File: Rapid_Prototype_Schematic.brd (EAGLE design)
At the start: 142 x 95 mm, 169 parts, among them IC2 SI4459ADY-T1-GE3, IC8 SI4485DY-T1-GE3, J1 XT60-M, J10 XT60-M, J2 XT60-M, J3 Vertical Qwiic Connector, J4 UJ2-MIBH-2-SMT-TR-67, J5 XT60-M, J6 XT60-M, J7 XT60-M, J8 XT60-M, J9 XT60-M, Q1 LTV-8141S, Q10 SI4435DDY, Q11 DMN65D8LFB-7, Q12 SI4435DDY, Q13 DMN65D8LFB-7, Q14 SI4435DDY, Q15 DMN65D8LFB-7, Q16 2N7002PW, Q2 2N7002PW, Q3 DMN65D8LFB-7, Q4 SI4435DDY, Q5 DMN65D8LFB-7, Q6 SI4435DDY, Q7 DMN65D8LFB-7, Q8 SI4435DDY, Q9 DMN65D8LFB-7, U1 LM35DM, U2 LM2904ITPX/NOPB, U3 LM2904ITPX/NOPB, U4 LM2904ITPX/NOPB, U5 LM2904ITPX/NOPB, U6 LM2904ITPX/NOPB, U7 TLV1117LV33DCYR, U8 LT1374IS8-5PBF

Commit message: Added Regulator Library, and Regulator to the Level shifter
Changed 5 volt traces from 0.008 to 0.02 for more flow.
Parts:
- removed L3: 10μH, SparkFun-Coils:0805
- added L1: SRR1206-5R0ML, INDUCTOR_SRR1240:IND_BOURNS_SRR1240
- moved C34 5.08 mm to (54.5, 22.5)
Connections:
- net 5V: now also L1.1; no longer L3.2
- net N$3: now also L1.2; no longer L3.1
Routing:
- net 5V: track 387.7 -> 370.4 mm, vias 13 -> 14
- net TETHER_A: track 83.7 -> 86.9 mm

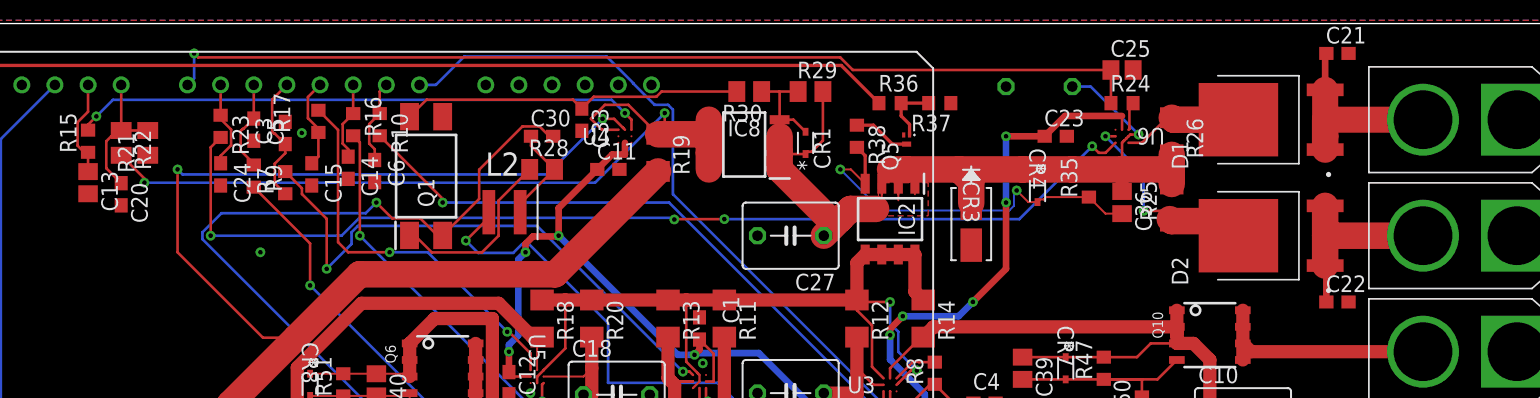
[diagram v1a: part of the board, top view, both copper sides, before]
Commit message: POLYGONS!!!
worked on creating polygons for the high current traces
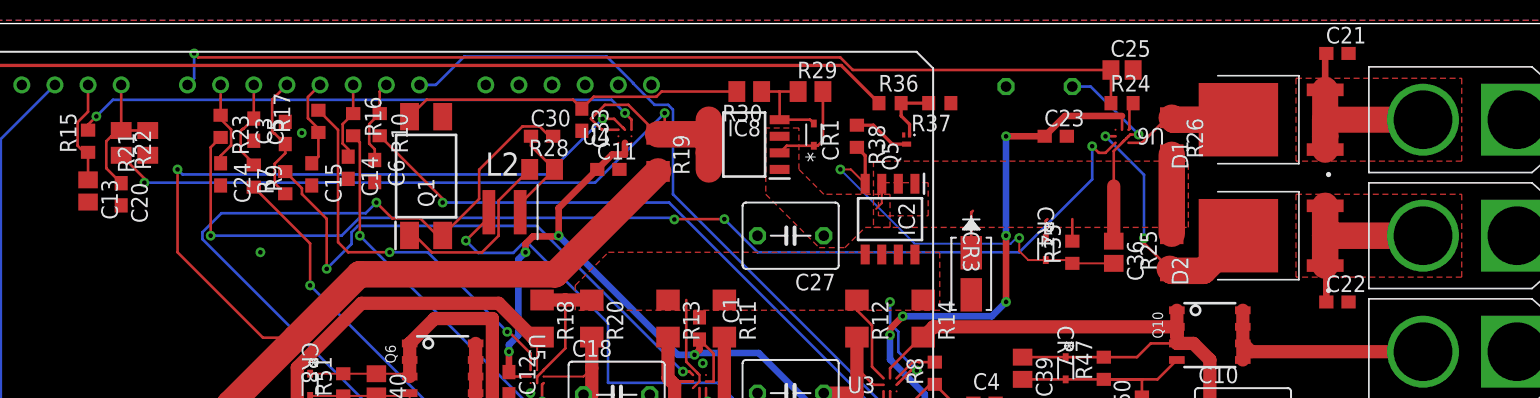
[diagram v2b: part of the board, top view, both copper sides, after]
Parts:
- moved R35 5.24 mm to (101.6, 77.5)
- moved CR4 4.49 mm to (99.6, 77.7)
- moved C36 3.86 mm to (104.8, 77.5)
- moved CR3 3.81 mm to (93.9, 75.8)
- moved R25 3.81 mm to (109.2, 77.5)
- moved CR1 0.90 mm to (81.8, 86.5)
- moved C13 0.64 mm to (26.2, 82.2)
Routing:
- net ESC_POWER: track 67.6 -> 33.6 mm
- net COMBINED_POWER: track 72.2 -> 39.3 mm
- net ESC_POWER2: track 16.0 -> 19.6 mm
- net N$34: track 80.7 -> 84.3 mm
- net 5V: track 370.4 -> 371.9 mm
- net ELEC_CURR: track 7.50 -> 8.17 mm
- added copper zone on layer 1, net ESC_POWER
- added copper zone on layer 1, net P_BATT+
- added copper zone on layer 1, net S_BATT+

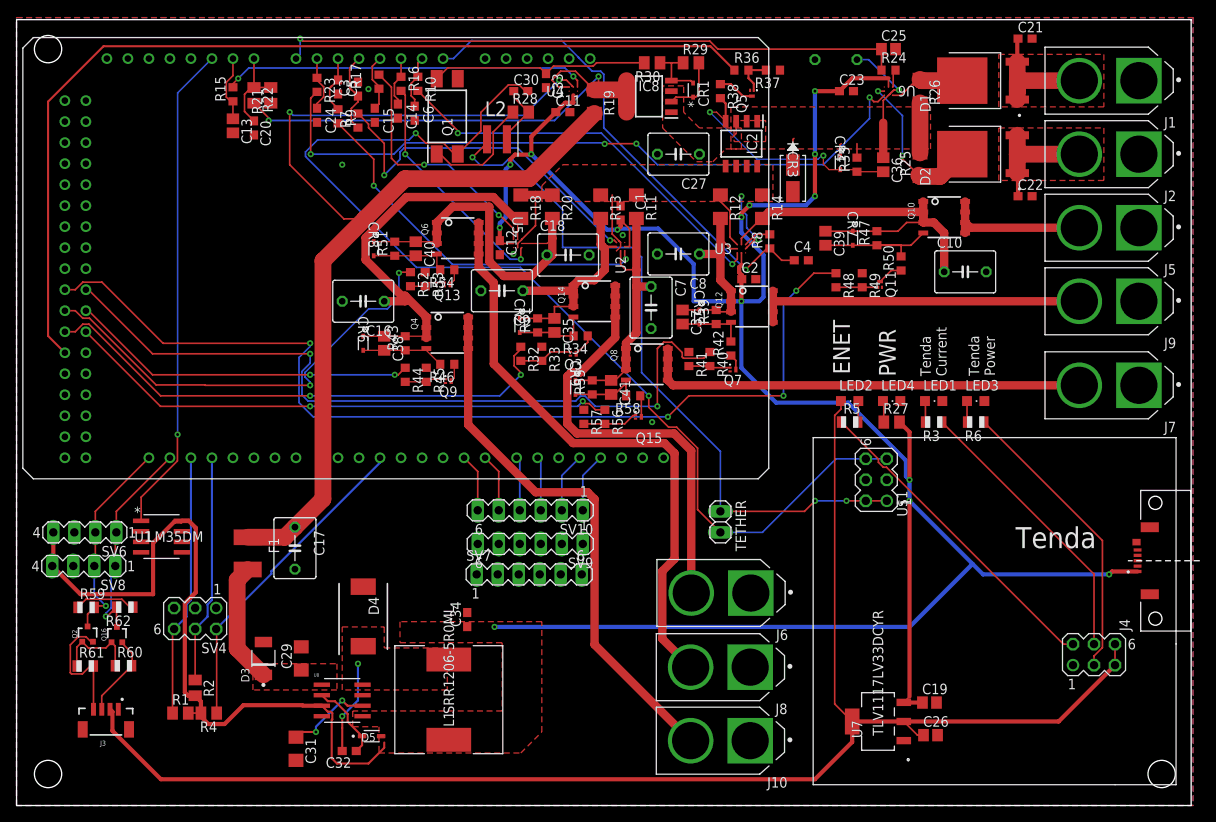
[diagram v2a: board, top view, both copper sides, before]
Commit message: Labeling and Part Replacing and GPIO LEDs
Switched PWM header with a different part, started labelling ESC's and added Software LED's
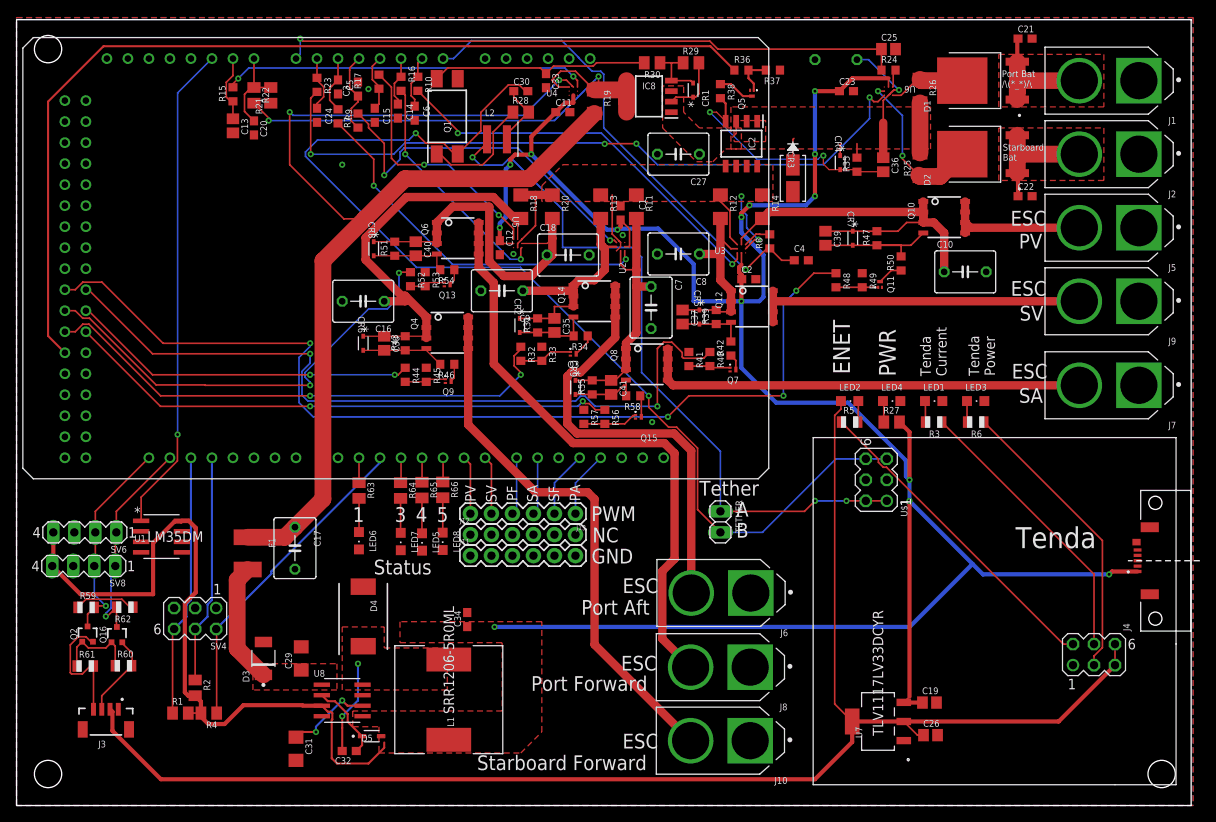
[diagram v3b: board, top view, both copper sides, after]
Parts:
- removed SV10: J10, con-lstb:MA06-1
- removed SV7: J7, con-lstb:MA06-1
- removed SV9: J9, con-lstb:MA06-1
- added J11, J12, J13: (no value), SparkFun-Connectors:1X06
- added LED5, LED6, LED7, LED8: GREEN, adafruit:CHIPLED_0805
- added R63, R64, R65, R66: 1k Ω, adafruit:M0805
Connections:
- new net N$14: $2_3_$_2020-06-04_21-52-10.4, R65.1
- new net N$28: $2_3_$_2020-06-04_21-52-10.5, R66.1
- new net N$40: $2_3_$_2020-06-04_21-52-10.1, R63.1
- new net N$41: LED6.A, R63.2
- new net N$42: LED7.A, R64.2
- new net N$45: LED5.A, R65.2
- new net N$46: LED8.A, R66.2
- new net N$8: $2_3_$_2020-06-04_21-52-10.3, R64.1
- net ESCPA_PWM: now also J13.1; no longer SV10.1
- net ESCPF_PWM: now also J13.4; no longer SV10.4
- net ESCPV_PWM: now also J13.6; no longer SV10.6
- net ESCSA_PWM: now also J13.3; no longer SV10.3
- net ESCSF_PWM: now also J13.2; no longer SV10.2
- net ESCSV_PWM: now also J13.5; no longer SV10.5
- net GND: now also J11.1, J11.2, J11.3, J11.4, J11.5, J11.6, LED5.C, LED6.C, LED7.C, LED8.C; no longer SV7.1, SV7.2, SV7.3, SV7.4, SV7.5, SV7.6
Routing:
- net N$45: track 0.00 -> 4.28 mm
- net N$46: track 0.00 -> 4.22 mm
- net N$42: track 0.00 -> 4.18 mm
- net N$41: track 0.00 -> 4.07 mm
- net N$8: track 0.00 -> 3.03 mm
- net N$40: track 0.00 -> 3.01 mm
- net N$14: track 0.00 -> 2.96 mm
- net N$28: track 0.00 -> 2.94 mm
- net ESCSF_PWM: track 7.24 -> 8.01 mm
- net ESCPA_PWM: track 7.24 -> 8.01 mm
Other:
- board text added: "1"
- board text added: "3"
- board text added: "4"
- board text added: "5"
- board text added: "A"
- board text added: "B"
- board text added: "ESC"
- board text added: "GND"
- board text added: "NC"
- board text added: "PA"
- board text added: "PF"
- board text added: "PV"
- board text added: "PWM"
- board text added: "Port Aft"
- board text added: "Port Bat /\\(*_*)/\\"
- board text added: "Port Forward"
- board text added: "SA"
- board text added: "SF"
- board text added: "SV"
- board text added: "Starboard Bat"
- board text added: "Starboard Forward"
- board text added: "Status"
- board text added: "Tether"

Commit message: Update Rapid_Prototype_Schematic.brd
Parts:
- moved CR8 5.52 mm to (47.8, 70.4), turned to 180 degrees
- moved TETHER 3.94 mm to (88.9, 35.3)
- moved C9 3.45 mm to (62.0, 61.2)
- moved R32 2.45 mm to (63.0, 53.2), turned to 90 degrees
- moved R33 2.06 mm to (65.0, 53.2), turned to 90 degrees
- moved CR3 2.03 mm to (93.9, 77.9)
- moved R31 1.78 mm to (63.0, 56.3)
- moved C35 1.27 mm to (65.0, 56.8)
- moved C18 1.07 mm to (67.7, 66.5)
- moved CR2 1.05 mm to (60.6, 57.0)
- moved R51 0.72 mm to (46.4, 67.3)
- moved U5 0.42 mm to (60.8, 67.6)
- moved C40 0.35 mm to (48.6, 67.3)
- moved C2 0.25 mm to (88.8, 63.6)
- moved R41 0.22 mm to (81.5, 54.1)
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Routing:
- net ESCSF_POWER: track 66.0 -> 70.8 mm
- net TETHER_B: track 132.4 -> 137.1 mm
- net TETHER_A: track 86.9 -> 83.3 mm
- net ESC_PA_POWER: track 31.5 -> 28.2 mm
- net ESC_SV_POWER: track 25.2 -> 22.6 mm
- net COMBINED_POWER: track 39.3 -> 37.2 mm
- net N$10: track 6.44 -> 4.41 mm
- net ESCPA_SWITCH: track 64.2 -> 62.3 mm
- net ESCPV_SWITCH: track 120.2 -> 121.9 mm
- net N$5: track 48.5 -> 50.2 mm
- net N$12: track 9.80 -> 11.3 mm
- net ESC_PV_POWER: track 47.3 -> 48.6 mm
- net N$2: track 28.6 -> 29.8 mm
- net ESCPF_POWER: track 72.1 -> 73.3 mm
- net ESC_SF_POWER: track 51.1 -> 49.9 mm
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
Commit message: Update Rapid_Prototype_Schematic.brd
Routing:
- net ESC_PF_POWER: track 42.4 -> 41.4 mm
- net ESC_POWER: track 33.8 -> 34.6 mm
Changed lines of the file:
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@@
 <vertex x="66.04" y="77.47"/>
 </polygon>
-<wire x1="60.9774" y1="67.259203125" x2="60.833" y2="67.114803125" width="0.2032" layer="1"/>
-<wire x1="60.9774" y1="67.76210625" x2="60.9774" y2="67.259203125" width="0.2032" layer="1"/>
 <wire x1="62.738" y1="69.519803125" x2="61.899796875" y2="68.6816" width="0.2032" layer="1"/>
 <wire x1="61.899796875" y1="68.6816" x2="61.89689375" y2="68.6816" width="0.2032" layer="1"/>
-<wire x1="61.89689375" y1="68.6816" x2="60.9774" y2="67.76210625" width="0.2032" layer="1"/>
-<wire x1="60.833" y1="67.114803125" x2="61.333" y2="68.114803125" width="0" layer="19" extent="1-1"/>
+<wire x1="61.89689375" y1="68.6816" x2="60.833" y2="67.61770625" width="0.2032" layer="1"/>
+<wire x1="60.833" y1="67.61770625" x2="60.833" y2="67.114803125" width="0.2032" layer="1"/>
+<wire x1="61.333" y1="68.114803125" x2="60.835903125" y2="67.61770625" width="0.2032" layer="1"/>
+<wire x1="60.835903125" y1="67.61770625" x2="60.833" y2="67.61770625" width="0.2032" layer="1"/>
 </signal>
 <signal name="N$1">
@@
 <wire x1="64.77" y1="68.58" x2="64.77" y2="70.968" width="2.032" layer="1"/>
 <wire x1="64.77" y1="68.58" x2="64.516" y2="68.326" width="0.1524" layer="1"/>
-<wire x1="64.516" y1="68.326" x2="63.804803125" y2="67.614803125" width="0.1524" layer="1"/>
 <wire x1="64.77" y1="66.548" x2="65.2043375" y2="66.548" width="1.016" layer="1"/>
 <wire x1="64.77" y1="66.548" x2="62.23" y2="64.008" width="2.032" layer="1"/>

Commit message: Update Rapid_Prototype_Schematic.brd
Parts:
- flipped C28 to the top
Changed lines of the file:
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@@
 <attribute name="VALUE" x="83.185" y="80.899" size="1.27" layer="27" ratio="10" rot="R180"/>
 </element>
-<element name="C28" library="adafruit" library_urn="urn:adsk.eagle:library:420" package="C050-050X075" package3d_urn="urn:adsk.eagle:package:6240360/1" value="220µF" x="99.06" y="90.17" smashed="yes" rot="MR0">
-<attribute name="NAME" x="102.489" y="93.091" size="1.27" layer="26" ratio="10" rot="MR0"/>
-<attribute name="VALUE" x="102.235" y="88.011" size="1.27" layer="28" ratio="10" rot="MR0"/>
+<element name="C28" library="adafruit" library_urn="urn:adsk.eagle:library:420" package="C050-050X075" package3d_urn="urn:adsk.eagle:package:6240360/1" value="220µF" x="99.06" y="90.17" smashed="yes">
+<attribute name="NAME" x="95.631" y="93.091" size="1.27" layer="25" ratio="10"/>
+<attribute name="VALUE" x="95.885" y="88.011" size="1.27" layer="27" ratio="10"/>
 </element>
 <element name="C29" library="adafruit" library_urn="urn:adsk.eagle:library:420" package="C1206" package3d_urn="urn:adsk.eagle:package:6240335/1" value="22uF" x="34.417" y="17.78" smashed="yes" rot="R90">
@@
 <wire x1="82.484" y1="89.789" x2="82.484" y2="86.03315" width="0.2032" layer="1"/>
 <wire x1="104.775" y1="82.55" x2="104.775" y2="78.32" width="1.016" layer="1"/>
-<wire x1="105.41" y1="85.86" x2="104.775" y2="85.225" width="0.2032" layer="1"/>
-<wire x1="104.775" y1="85.225" x2="104.775" y2="82.55" width="0.2032" layer="1"/>
+<wire x1="105.41" y1="85.86" x2="105.41" y2="85.606" width="0.2032" layer="1"/>
+<wire x1="105.41" y1="85.606" x2="104.775" y2="84.971" width="0.2032" layer="1"/>
+<wire x1="104.775" y1="84.971" x2="104.775" y2="82.55" width="0.2032" layer="1"/>
 <wire x1="105.91" y1="86.36" x2="105.7656" y2="86.2156" width="0.2032" layer="1"/>
 <wire x1="105.7656" y1="86.2156" x2="105.7627" y2="86.2156" width="0.2032" layer="1"/>
@@
 <wire x1="106.0422" y1="86.4922" x2="106.68" y2="86.4922" width="0.2032" layer="1"/>
 <via x="106.68" y="86.4922" extent="1-16" drill="0.35"/>
-<wire x1="106.68" y1="86.4922" x2="103.0022" y2="90.17" width="0.2032" layer="16"/>
-<wire x1="103.0022" y1="90.17" x2="101.6" y2="90.17" width="0.2032" layer="16"/>
 <wire x1="86.55896875" y1="80.7911" x2="86.995" y2="81.22713125" width="0.1524" layer="1"/>
 <wire x1="86.995" y1="81.22713125" x2="86.995" y2="82.722" width="0.1524" layer="1"/>
@@
 <vertex x="87.63" y="79.375"/>
 </polygon>
+<wire x1="96.52" y1="90.17" x2="94.8718" y2="88.5218" width="0.2032" layer="1"/>
+<wire x1="94.8718" y1="88.5218" x2="94.8718" y2="83.919359375" width="0.2032" layer="1"/>
 </signal>
 <signal name="N$3">

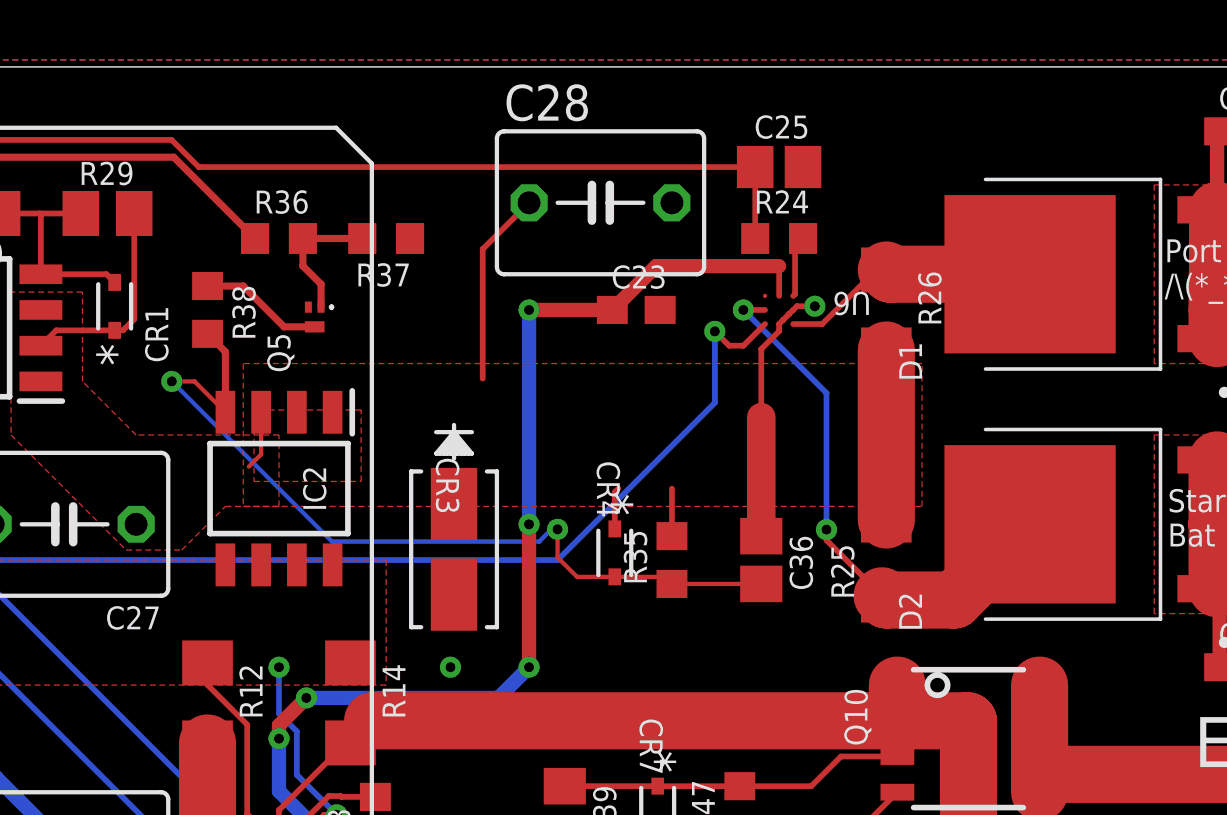
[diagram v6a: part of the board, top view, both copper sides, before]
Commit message: Resistor value change
Changed the values for the resistors. Increased the size of resistors R25 and R26.
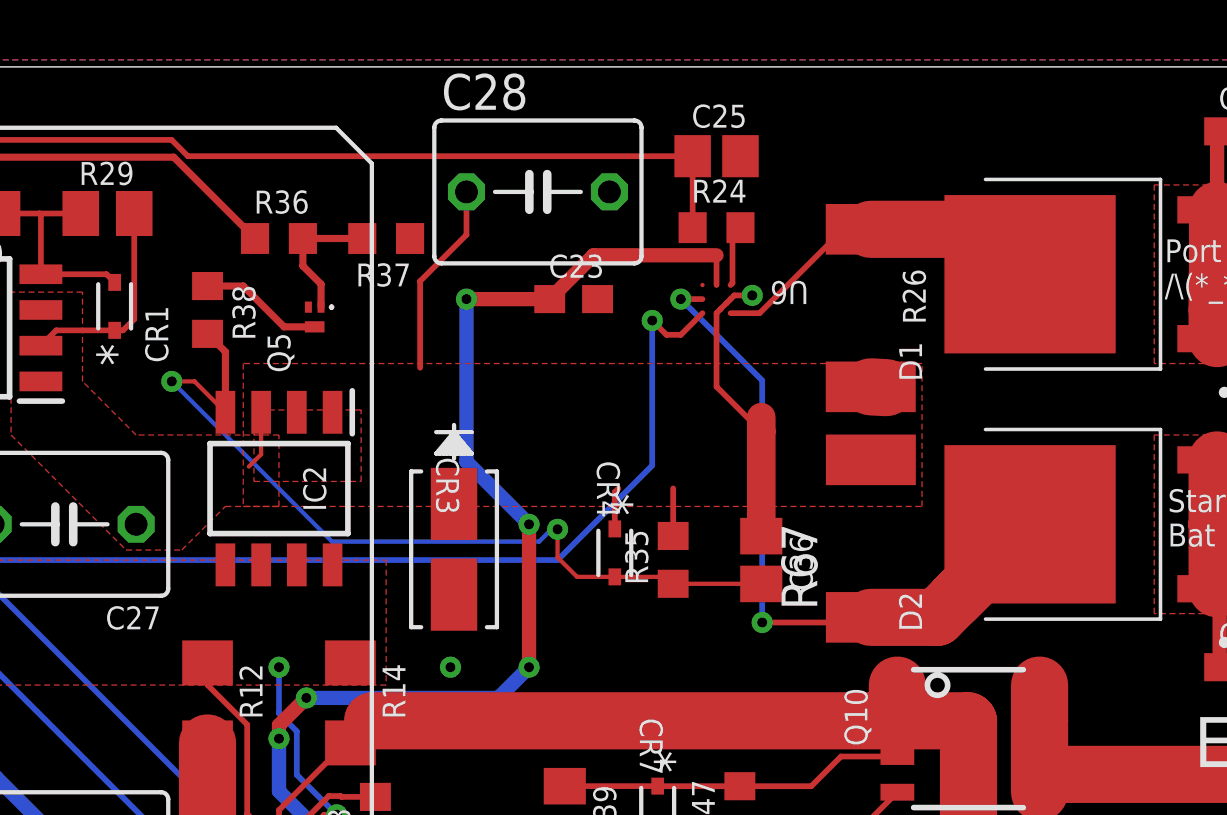
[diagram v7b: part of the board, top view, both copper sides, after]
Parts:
- removed R25: 0.005Ω 1%, adafruit:R1206
- added R67: 0.8Ω 1%, rcl:R2512
- R13, R14, R20: value 0.005 -> 0.003
- R19: value 0.010Ω -> 0.003Ω
- R26: value 0.005Ω 1% -> 0.8Ω 1%; device adafruit:R1206 -> rcl:R2512
- moved C28 2.26 mm to (96.8, 90.6)
- moved C23 2.26 mm to (98.1, 86.7)
- moved C25 2.26 mm to (103.2, 91.8)
- moved R24 2.26 mm to (103.2, 89.3)
- moved U6 2.26 mm to (103.2, 86.7)
- moved R26 0.56 mm to (108.7, 86.4)
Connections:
- net COMBINED_POWER: now also R67.2; no longer R25.2
- net ESC_POWER2: now also R67.1; no longer R25.1
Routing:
- net ESC_POWER2: track 19.6 -> 28.2 mm
- net COMBINED_POWER: track 37.6 -> 33.4 mm
- net ESC_POWER1: track 9.28 -> 12.5 mm
- net STBD_BAT_CURR: track 76.0 -> 73.6 mm
- net 5V: track 371.5 -> 372.8 mm
- net N$34: track 84.3 -> 83.7 mm
